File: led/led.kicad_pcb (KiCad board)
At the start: 2 copper layers, 18 parts

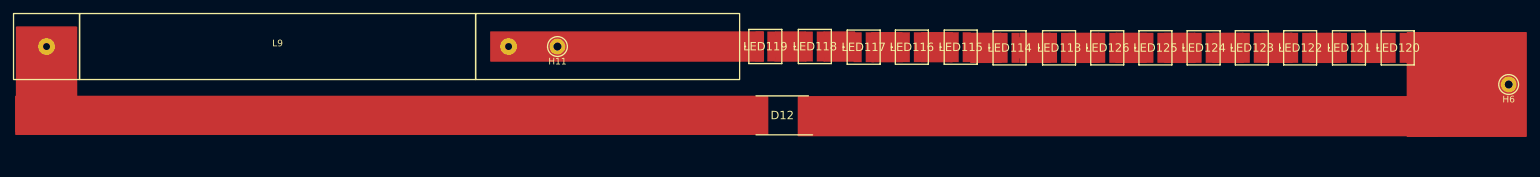
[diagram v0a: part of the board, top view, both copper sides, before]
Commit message: purging unused symbols and footprints
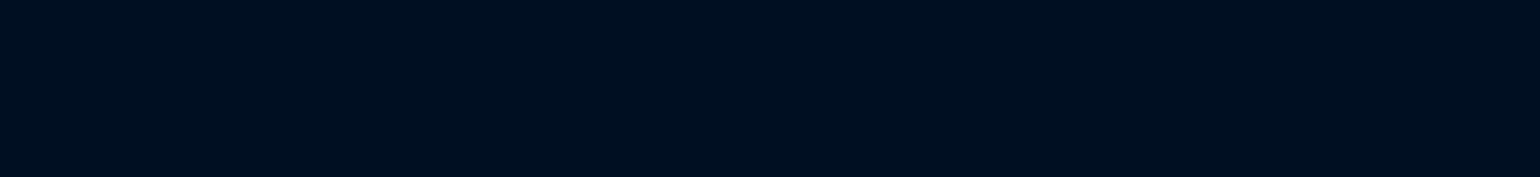
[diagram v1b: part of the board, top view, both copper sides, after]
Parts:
- removed D12: zener, arduino-library:DIOM7959X262N
- removed H11, H6: MountingHole_Pad, Connector_Pin:Pin_D1.0mm_L10.0mm_LooseFit
- removed L9: 220 uH @5.8A, arduino-library:Coil_6cmx1cm
- removed LED113, LED114, LED115, LED116, LED117, LED118, LED119, LED120, LED121, LED122, LED123, LED124, LED125, LED126: L150-65705024000H0, arduino-library:L15065705024000H0
